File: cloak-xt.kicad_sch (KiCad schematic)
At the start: 42 parts, among them J1 JST, J2 Conn_01x02, U1 STM32F072CBT6

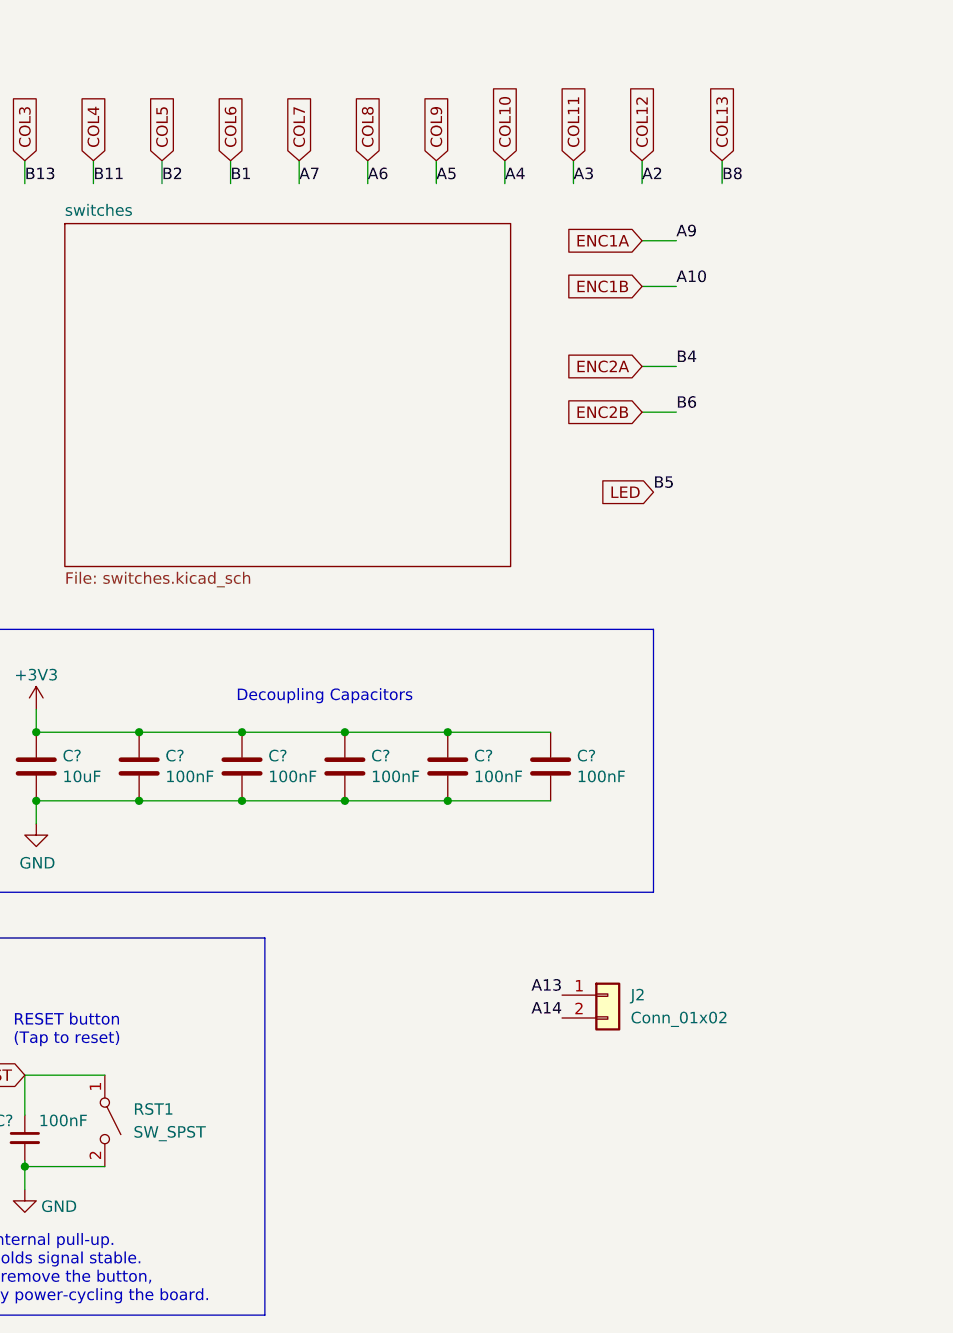
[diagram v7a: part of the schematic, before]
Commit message: Add pins breakout
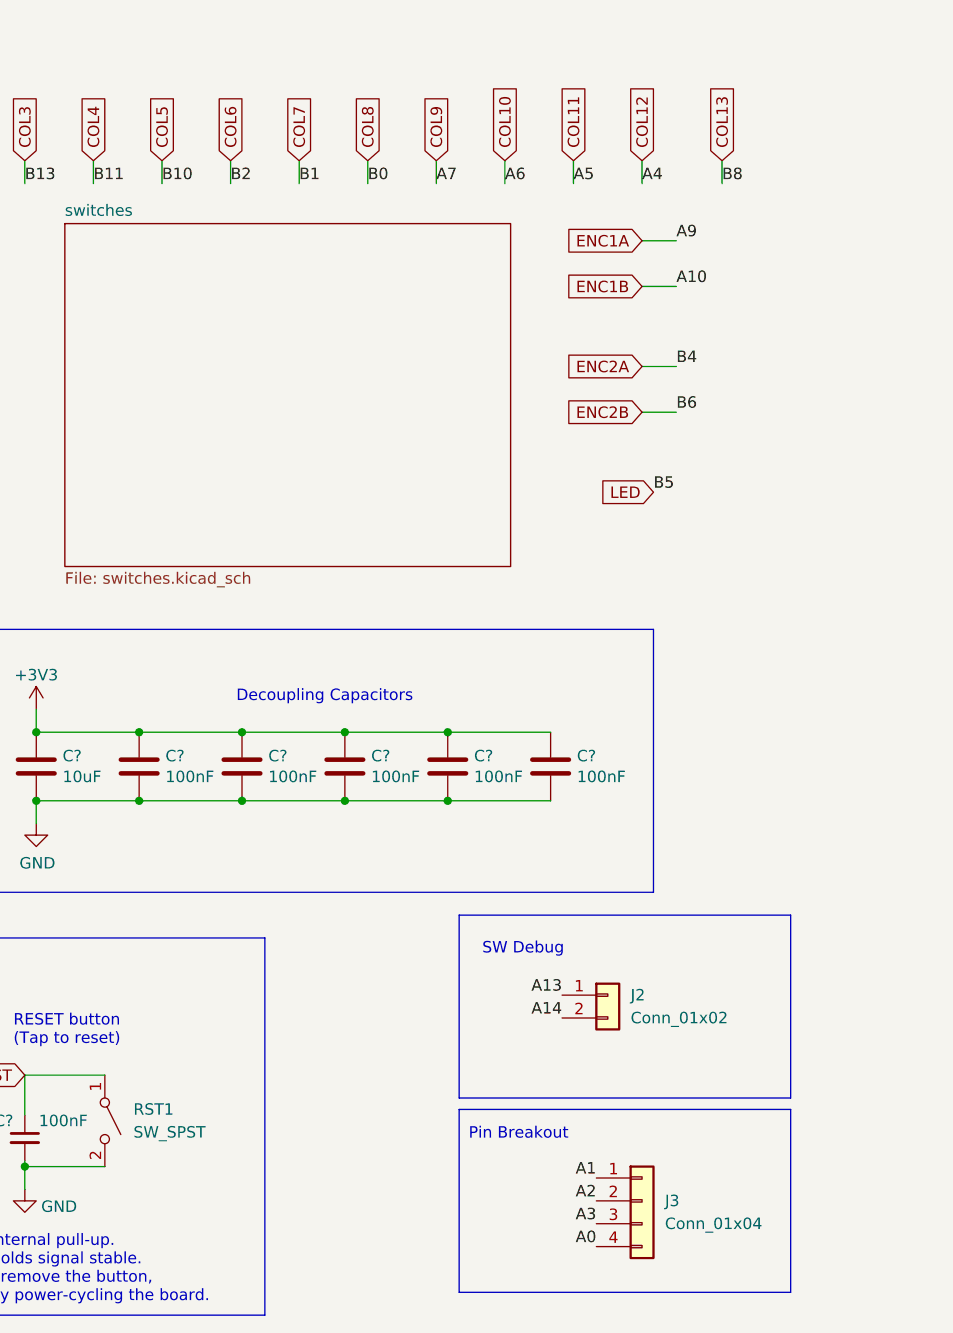
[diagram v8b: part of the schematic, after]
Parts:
- added J3: Conn_01x04, Connector_PinHeader_1.00mm:PinHeader_1x04_P1.00mm_Vertical, symbol Connector_Generic:Conn_01x04
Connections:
- net B0 is gone; now on net COL8: U1.18 (PB0)
- net B10 is gone; now on net COL5: U1.21 (PB10)
- net A0: now also J3.4 (Pin_4)
- net A1: now also J3.1 (Pin_1)
- net COL10: now also U1.16 (PA6); no longer U1.14 (PA4)
- net COL11: now also U1.15 (PA5); no longer U1.13 (PA3)
- net COL12: now also U1.14 (PA4); no longer U1.12 (PA2)
- net COL5: no longer U1.20 (PB2)
- net COL6: now also U1.20 (PB2); no longer U1.19 (PB1)
- net COL7: now also U1.19 (PB1); no longer U1.17 (PA7)
- net COL8: no longer U1.16 (PA6)
- net COL9: now also U1.17 (PA7); no longer U1.15 (PA5)
- new net A2: J3.2 (Pin_2), U1.12 (PA2)
- new net A3: J3.3 (Pin_3), U1.13 (PA3)
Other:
- note added: "Pin Breakout"
- note added: "SW Debug"
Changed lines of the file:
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@@
 	)
 	(rectangle
+		(start 234.95 138.43)
+		(end 271.78 158.75)
+		(stroke
+			(width 0)
+			(type default)
+		)
+		(fill
+			(type none)
+		)
+	)
+	(rectangle
 		(start 64.77 123.19)
 		(end 112.395 155.575)
@@
 	)
 	(rectangle
+		(start 234.95 116.84)
+		(end 271.78 137.16)
+		(stroke
+			(width 0)
+			(type default)
+		)
+		(fill
+			(type none)
+		)
+	)
+	(rectangle
 		(start 115.57 119.38)
 		(end 213.36 161.29)
@@
 		)
 	)
+	(text "Pin Breakout"
+		(exclude_from_sim no)
+		(at 241.554 141.224 0)
+		(effects
+			(font
+				(size 1.27 1.27)
+			)
+		)
+	)
 	(text "FT/TIM1_CH3/USART1_RX"
 		(exclude_from_sim no)
@@
 		)
 	)
+	(text "SW Debug"
+		(exclude_from_sim no)
+		(at 242.062 120.65 0)
+		(effects
+			(font
+				(size 1.27 1.27)
+			)
+		)
+	)
 	(text "TTa/TIM3_CH1/SPI1_MISO/ADC_IN6"
 		(exclude_from_sim no)
@@
 	)
 	(label "B1"
-		(at 209.55 35.56 0)
+		(at 217.17 35.56 0)
 		(fields_autoplaced yes)
 		(effects
@@
 		)
 	)
+	(label "A1"
+		(at 250.19 146.05 180)
+		(fields_autoplaced yes)
+		(effects
+			(font
+				(size 1.27 1.27)
+			)
+			(justify right bottom)
+		)
+	)
 	(label "A7"
-		(at 217.17 35.56 0)
+		(at 232.41 35.56 0)
 		(fields_autoplaced yes)
 		(effects
@@
 	)
 	(label "A5"
-		(at 232.41 35.56 0)
+		(at 247.65 35.56 0)
+		(fields_autoplaced yes)
+		(effects
+			(font
+				(size 1.27 1.27)
+			)
+			(justify left bottom)
+		)
+	)
+	(label "B10"
+		(at 201.93 35.56 0)
 		(fields_autoplaced yes)
 		(effects
@@
 		)
 	)
+	(label "B0"
+		(at 224.79 35.56 0)
+		(fields_autoplaced yes)
+		(effects
+			(font
+				(size 1.27 1.27)
+			)
+			(justify left bottom)
+		)
+	)
 	(label "B14"
 		(at 60.96 93.98 180)
@@
 		)
 	)
+	(label "A0"
+		(at 250.19 153.67 180)
+		(fields_autoplaced yes)
+		(effects
+			(font
+				(size 1.27 1.27)
+			)
+			(justify right bottom)
+		)
+	)
 	(label "B0"
 		(at 60.96 58.42 180)
@@
 	)
 	(label "A4"
-		(at 240.03 35.56 0)
+		(at 255.27 35.56 0)
 		(fields_autoplaced yes)
 		(effects
@@
 	)
 	(label "A6"
-		(at 224.79 35.56 0)
+		(at 240.03 35.56 0)
 		(fields_autoplaced yes)
 		(effects
@@
 	)
 	(label "A3"
-		(at 247.65 35.56 0)
+		(at 250.19 151.13 180)
 		(fields_autoplaced yes)
 		(effects
@@
 				(size 1.27 1.27)
 			)
-			(justify left bottom)
+			(justify right bottom)
 		)
 	)
@@
 	)
 	(label "A2"
-		(at 255.27 35.56 0)
+		(at 250.19 148.59 180)
 		(fields_autoplaced yes)
 		(effects
@@
 				(size 1.27 1.27)
 			)
-			(justify left bottom)
+			(justify right bottom)
 		)
 	)
 	(label "B2"
-		(at 201.93 35.56 0)
+		(at 209.55 35.56 0)
 		(fields_autoplaced yes)
 		(effects
@@
 					(unit 1)
 				)
+			)
+		)
+	)
+	(symbol
+		(lib_id "Connector_Generic:Conn_01x04")
+		(at 255.27 148.59 0)
+		(unit 1)
+		(exclude_from_sim no)
+		(in_bom yes)
+		(on_board yes)
+		(dnp no)
+		(fields_autoplaced yes)
+		(property "Reference" "J3"
+			(at 257.81 148.5899 0)
+			(effects
+				(font
+					(size 1.27 1.27)
+				)
+				(justify left)
+			)
+		)
+		(property "Value" "Conn_01x04"
+			(at 257.81 151.1299 0)
+			(effects
+				(font
+					(size 1.27 1.27)
+				)
+				(justify left)
+			)
+		)
+		(property "Footprint" "Connector_PinHeader_1.00mm:PinHeader_1x04_P1.00mm_Vertical"
+			(at 255.27 148.59 0)
+			(effects
+				(font
+					(size 1.27 1.27)
+				)
+				(hide yes)
+			)
+		)
+		(property "Datasheet" "~"
+			(at 255.27 148.59 0)
+			(effects
+				(font
+					(size 1.27 1.27)
+				)
+				(hide yes)
+			)
+		)
+		(property "Description" "Generic connector, single row, 01x04, script generated (kicad-library-utils/schlib/autogen/connector/)"
+			(at 255.27 148.59 0)
+			(effects
+				(font
+					(size 1.27 1.27)
+				)
+				(hide yes)
+			)
+		)
+		(pin "4"
+		)
+		(pin "2"
+		)
+		(pin "3"
+		)
+		(pin "1"
+		)
+		(instances
+			(project ""
+				(path "/4d291fcf-fdf2-46ba-aa57-60bc75f9cc32"
+					(reference "J3")
+					(unit 1)
+				)
